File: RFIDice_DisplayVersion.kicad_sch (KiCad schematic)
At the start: 77 parts, among them J1 Conn_01x02, J2 CORTEX_JTAG_DEBUG_MINIMUM_PTH, Q1 Q_NMOS_DGS, SW1 OS102011MA1Q, SW2 SW_Push, SW3 SW_Push, SW4 SW_Push, SW5 SW_Push, SW6 SW_Push, SW7 SW_Push, SW8 SW_Push, SW9 SW_Push, U1 MCP73831T-2ACI/OT, U2 PN532, U3 LM4040DBZ-3, U4 R3111N-SOT-23-5, U5 TPS7A2133PYWDJ, U6 RP2040, U7 W25Q128JVS, U8 Display, X1 USB_C, Y1 ABLS-12.000MHZ-B4-T

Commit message: StartedPCBWork
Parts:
- removed C17: 4.7µF, Capacitor_SMD:C_0603_1608Metric_Pad1.08x0.95mm_HandSolder, symbol AndySeniorProjSymbols:C
- removed R7: 470kΩ, Resistor_SMD:R_0603_1608Metric_Pad0.98x0.95mm_HandSolder, symbol AndySeniorProjSymbols:R
- removed SW7, SW8, SW9: SW_Push, AndySeniorProjectFootprints:EVP-ASDC1A_Tactile_PushButton, symbol Switch:SW_Push
- removed TP1: TestPoint, TestPoint:TestPoint_Keystone_5000-5004_Miniature, symbol Connector:TestPoint
- removed U4: R3111N-SOT-23-5, Package_TO_SOT_SMD:SOT-23-5_HandSoldering, symbol AndySeniorProjSymbols:R3111N-SOT-23-5
- removed U5: TPS7A2133PYWDJ, AndySeniorProjectFootprints:TPS7A2133PYWDJ, symbol AndySeniorProjSymbols:TPS7A2133PYWDJ
- added R9: 470kΩ, Resistor_SMD:R_0603_1608Metric_Pad0.98x0.95mm_HandSolder, symbol AndySeniorProjSymbols:R
- added TP6, TP7: TestPoint, TestPoint:TestPoint_Keystone_5000-5004_Miniature, symbol Connector:TestPoint
- added U3: MIC5219-3.3YM5, Package_TO_SOT_SMD:SOT-23-5, symbol Regulator_Linear:MIC5219-3.3YM5
- BATT1: renamed from BT1; footprint AndySeniorProjectFootprints:AndyBattery -> JST2:JSTPH2
- C6: renamed from C20; footprint Capacitor_Tantalum_SMD:CP_EIA-3528-21_Kemet-B_Pad1.50x2.35mm_HandSolder -> Capacitor_SMD:C_1210_3225Metric_Pad1.33x2.70mm_HandSolder
- Q1: footprint Package_TO_SOT_SMD:SOT-23 -> Package_TO_SOT_SMD:SOT-23_Handsoldering
- SW6: renamed from SW1; value OS102011MA1Q -> (none)
- renumbered C7 to C10, C6 to C11, C4 to C12, C8 to C13, C10 to C14, C11 to C15, C12 to C16, C13 to C17, C14 to C18, C15 to C19, C21 to C2, C16 to C20, C18 to C3, C19 to C4, C2 to C5, C9 to C7, C3 to C8, C5 to C9, R15 to R1, R3 to R10, R4 to R11, R5 to R12, R6 to R13, R11 to R14, R12 to R15, R1 to R2, R2 to R3, R9 to R4, R10 to R5, R8 to R6, R13 to R7, R14 to R8, SW2 to SW1, SW3 to SW2, SW4 to SW3, SW5 to SW4, SW6 to SW5, TP2 to TP1, TP9 to TP10, TP10 to TP11, TP11 to TP12, TP14 to TP13, TP15 to TP14, TP16 to TP15, TP12 to TP16, TP13 to TP17, TP17 to TP18, TP4 to TP2, TP18 to TP3, TP5 to TP4, TP3 to TP5, TP7 to TP8, TP8 to TP9, U3 to U1, U1 to U2, U6 to U4, U8 to U5, U7 to U6, U2 to U7
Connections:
- net +3V3: now also U3.5 (OUT)
- net +BATT: now also SW6.1, U3.1 (IN), U3.3 (EN)
- net GND: now also U3.2 (GND)
- net GND1: no longer BATT1.2 (-), C5.2, C6.2, Q1.3 (S), R4.1, R5.1, SW6.3, TP1.1, X1.A1B12 (GND), X1.B1A12 (GND)
- net SPI_CS: now also U5.5 (TFT_CS); no longer U5.6 (Card_CS)
- net UART0_RX: now reaches U4.2 (GPIO0)
- net UART0_RX: now also TP6.1
- net UART0_TX: now reaches U4.3 (GPIO1)
- net UART0_TX: now also TP7.1
- net BATT_LOW_STAT: no longer names the net of Q1.2 (G), SW6.2
- net BATT_LOW_STAT: now also R9.1
- net BTN6: no longer names the net of U4.14 (GPIO11)
- net BTN7: no longer names the net of U4.15 (GPIO12)
- net BTN8: no longer names the net of U4.16 (GPIO13)
- new net -BATT: BATT1.2 (-), C5.2, C6.2, Q1.3 (S), R4.1, R5.1, R9.2, TP1.1, X1.A1B12 (GND), X1.B1A12 (GND)
- no-connect marks 20 -> 21
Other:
- note added: "Power Switch"
- note removed: "Battery Supervision Power Switch"
- moved on the sheet: BATT1, C12, C2, Q1, R1, SW1, SW2, SW3, SW4, SW5, SW6A, TP1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

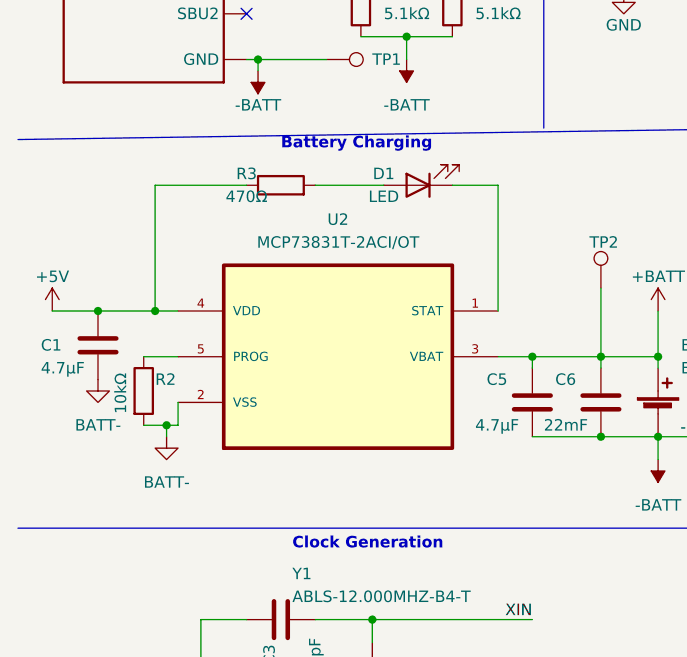
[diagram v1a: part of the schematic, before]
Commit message: Gonna go back and change start from power instead
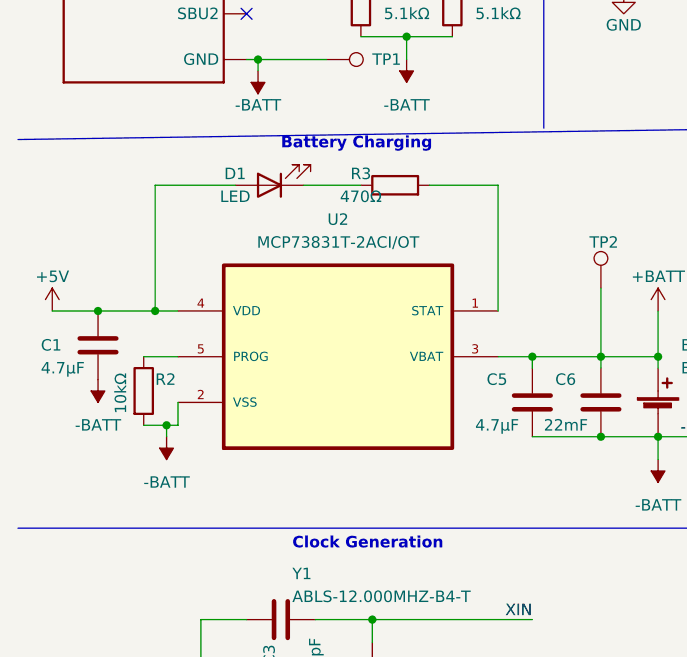
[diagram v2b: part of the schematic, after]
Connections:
- net GND1 is gone; now on net -BATT: C1.2, R2.2, U2.2 (VSS)
- net +5V: now also D1.2 (A); no longer R3.1
- net at R3.2: now also U2.1 (STAT); no longer D1.2 (A)
- net at D1.1 (K): now also R3.1; no longer U2.1 (STAT)
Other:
- moved on the sheet: D1, R3
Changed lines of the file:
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@@
+    (stroke (width 0) (type default) (color 0 0 0 0))
+  )
+  (wire (pts (xy 44.45 57.15) (xy 50.8 57.15))
     (stroke (width 0) (type default) (color 0 0 0 0))
   )
@@
     (stroke (width 0) (type default) (color 0 0 0 0))
   )
-  (wire (pts (xy 60.96 57.15) (xy 66.04 57.15))
-    (stroke (width 0) (type default) (color 0 0 0 0))
-  )
   (wire (pts (xy 199.39 55.88) (xy 199.39 59.69))
     (stroke (width 0) (type default) (color 0 0 0 0))
@@
     (stroke (width 0) (type default) (color 0 0 0 0))
   )
-  (wire (pts (xy 27.94 57.15) (xy 38.1 57.15))
+  (wire (pts (xy 58.42 57.15) (xy 66.04 57.15))
     (stroke (width 0) (type default) (color 0 0 0 0))
   )
@@
     (stroke (width 0) (type default) (color 0 0 0 0))
   )
-  (wire (pts (xy 45.72 57.15) (xy 53.34 57.15))
-    (stroke (width 0) (type default) (color 0 0 0 0))
-  )
   (wire (pts (xy 104.14 59.69) (xy 111.76 59.69))
     (stroke (width 0) (type default) (color 0 0 0 0))
@@
   )
   (wire (pts (xy 234.95 139.7) (xy 234.95 151.13))
+    (stroke (width 0) (type default) (color 0 0 0 0))
+  )
+  (wire (pts (xy 27.94 57.15) (xy 36.83 57.15))
     (stroke (width 0) (type default) (color 0 0 0 0))
   )
@@
     (pin "1")
   )
-  (symbol (lib_id "AndySeniorProjSymbols:R") (at 41.91 57.15 90) (unit 1)
-    (in_bom yes) (on_board yes)
-    (property "Reference" "R3" (id 0) (at 38.1 55.88 90))
-    (property "Value" "470Ω" (id 1) (at 38.1 58.42 90))
-    (property "Footprint" "Resistor_SMD:R_0603_1608Metric_Pad0.98x0.95mm_HandSolder" (id 2) (at 41.91 58.928 90)
-      (effects (font (size 1.27 1.27)) hide)
-    )
-    (property "Datasheet" "~" (id 3) (at 41.91 57.15 0)
+  (symbol (lib_id "AndySeniorProjSymbols:R") (at 54.61 57.15 90) (unit 1)
+    (in_bom yes) (on_board yes)
+    (property "Reference" "R3" (id 0) (at 50.8 55.88 90))
+    (property "Value" "470Ω" (id 1) (at 50.8 58.42 90))
+    (property "Footprint" "Resistor_SMD:R_0603_1608Metric_Pad0.98x0.95mm_HandSolder" (id 2) (at 54.61 58.928 90)
+      (effects (font (size 1.27 1.27)) hide)
+    )
+    (property "Datasheet" "~" (id 3) (at 54.61 57.15 0)
       (effects (font (size 1.27 1.27)) hide)
     )
@@
     (pin "1")
   )
+  (symbol (lib_id "power:-BATT") (at 21.59 78.74 180) (unit 1)
+    (in_bom yes) (on_board yes) (fields_autoplaced)
+    (property "Reference" "#PWR02" (id 0) (at 21.59 74.93 0)
+      (effects (font (size 1.27 1.27)) hide)
+    )
+    (property "Value" "-BATT" (id 1) (at 21.59 83.82 0))
+    (property "Footprint" "" (id 2) (at 21.59 78.74 0)
+      (effects (font (size 1.27 1.27)) hide)
+    )
+    (property "Datasheet" "" (id 3) (at 21.59 78.74 0)
+      (effects (font (size 1.27 1.27)) hide)
+    )
+    (pin "1")
+  )
   (symbol (lib_id "Connector:TestPoint") (at 203.2 101.6 0) (unit 1)
     (in_bom yes) (on_board yes)
@@
     (pin "1")
     (pin "2")
-  )
-  (symbol (lib_id "power:GND1") (at 21.59 78.74 0) (unit 1)
-    (in_bom yes) (on_board yes) (fields_autoplaced)
-    (property "Reference" "#PWR02" (id 0) (at 21.59 85.09 0)
-      (effects (font (size 1.27 1.27)) hide)
-    )
-    (property "Value" "BATT-" (id 1) (at 21.59 83.82 0))
-    (property "Footprint" "" (id 2) (at 21.59 78.74 0)
-      (effects (font (size 1.27 1.27)) hide)
-    )
-    (property "Datasheet" "" (id 3) (at 21.59 78.74 0)
-      (effects (font (size 1.27 1.27)) hide)
-    )
-    (pin "1")
-  )
-  (symbol (lib_id "power:GND1") (at 29.21 85.09 0) (unit 1)
-    (in_bom yes) (on_board yes)
-    (property "Reference" "#PWR05" (id 0) (at 29.21 91.44 0)
-      (effects (font (size 1.27 1.27)) hide)
-    )
-    (property "Value" "BATT-" (id 1) (at 29.21 90.17 0))
-    (property "Footprint" "" (id 2) (at 29.21 85.09 0)
-      (effects (font (size 1.27 1.27)) hide)
-    )
-    (property "Datasheet" "" (id 3) (at 29.21 85.09 0)
-      (effects (font (size 1.27 1.27)) hide)
-    )
-    (pin "1")
   )
   (symbol (lib_id "Connector:TestPoint") (at 213.36 143.51 90) (unit 1)
@@
     (pin "2")
   )
-  (symbol (lib_id "AndySeniorProjSymbols:LED") (at 57.15 57.15 180) (unit 1)
-    (in_bom yes) (on_board yes)
-    (property "Reference" "D1" (id 0) (at 53.34 55.88 0))
-    (property "Value" "LED" (id 1) (at 53.34 58.42 0))
-    (property "Footprint" "LED_SMD:LED_0603_1608Metric_Pad1.05x0.95mm_HandSolder" (id 2) (at 57.15 57.15 0)
-      (effects (font (size 1.27 1.27)) hide)
-    )
-    (property "Datasheet" "~" (id 3) (at 57.15 57.15 0)
+  (symbol (lib_id "AndySeniorProjSymbols:LED") (at 40.64 57.15 180) (unit 1)
+    (in_bom yes) (on_board yes)
+    (property "Reference" "D1" (id 0) (at 36.83 55.88 0))
+    (property "Value" "LED" (id 1) (at 36.83 58.42 0))
+    (property "Footprint" "LED_SMD:LED_0603_1608Metric_Pad1.05x0.95mm_HandSolder" (id 2) (at 40.64 57.15 0)
+      (effects (font (size 1.27 1.27)) hide)
+    )
+    (property "Datasheet" "~" (id 3) (at 40.64 57.15 0)
       (effects (font (size 1.27 1.27)) hide)
     )
@@
     )
     (property "Datasheet" "~" (id 3) (at 213.36 130.81 0)
+      (effects (font (size 1.27 1.27)) hide)
+    )
+    (pin "1")
+  )
+  (symbol (lib_id "power:-BATT") (at 29.21 85.09 180) (unit 1)
+    (in_bom yes) (on_board yes) (fields_autoplaced)
+    (property "Reference" "#PWR05" (id 0) (at 29.21 81.28 0)
+      (effects (font (size 1.27 1.27)) hide)
+    )
+    (property "Value" "-BATT" (id 1) (at 29.21 90.17 0))
+    (property "Footprint" "" (id 2) (at 29.21 85.09 0)
+      (effects (font (size 1.27 1.27)) hide)
+    )
+    (property "Datasheet" "" (id 3) (at 29.21 85.09 0)
       (effects (font (size 1.27 1.27)) hide)
     )
@@
       (reference "#PWR01") (unit 1) (value "+5V") (footprint "")
     )
-    (path "/782e0503-2e76-4af9-9173-bfa816098e50"
-      (reference "#PWR02") (unit 1) (value "BATT-") (footprint "")
+    (path "/3eeddd15-60f2-4db5-b227-f972c432796c"
+      (reference "#PWR02") (unit 1) (value "-BATT") (footprint "")
     )
     (path "/4ee43910-3ac2-41da-a684-a0f74945d0a4"
@@
       (reference "#PWR04") (unit 1) (value "GND") (footprint "")
     )
-    (path "/7b7632e0-1268-43a5-af7d-088c7d5052b1"
-      (reference "#PWR05") (unit 1) (value "BATT-") (footprint "")
+    (path "/f9146b49-efdb-4af9-a35c-3cbe45fd55c2"
+      (reference "#PWR05") (unit 1) (value "-BATT") (footprint "")
     )
     (path "/a0bdbfdb-7966-4d51-810c-7ab6910b5a79"

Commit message: Maybe probably finished
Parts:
- removed TP14, TP15, TP18, TP3: TestPoint, TestPoint:TestPoint_Keystone_5000-5004_Miniature, symbol Connector:TestPoint
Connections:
- net BTN1: now also U4.34 (GPIO22); no longer U4.8 (GPIO6)
- net BTN2: now also U4.35 (GPIO23); no longer U4.9 (GPIO7)
- net BTN3: now also U4.36 (GPIO24); no longer U4.11 (GPIO8)
- net BTN4: now also U4.37 (GPIO25); no longer U4.12 (GPIO9)
- net BTN5: now also U4.39 (GPIO27_ADC1); no longer U4.13 (GPIO10)
